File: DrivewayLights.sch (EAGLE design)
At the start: 29 parts, among them U1 TLC59108PW

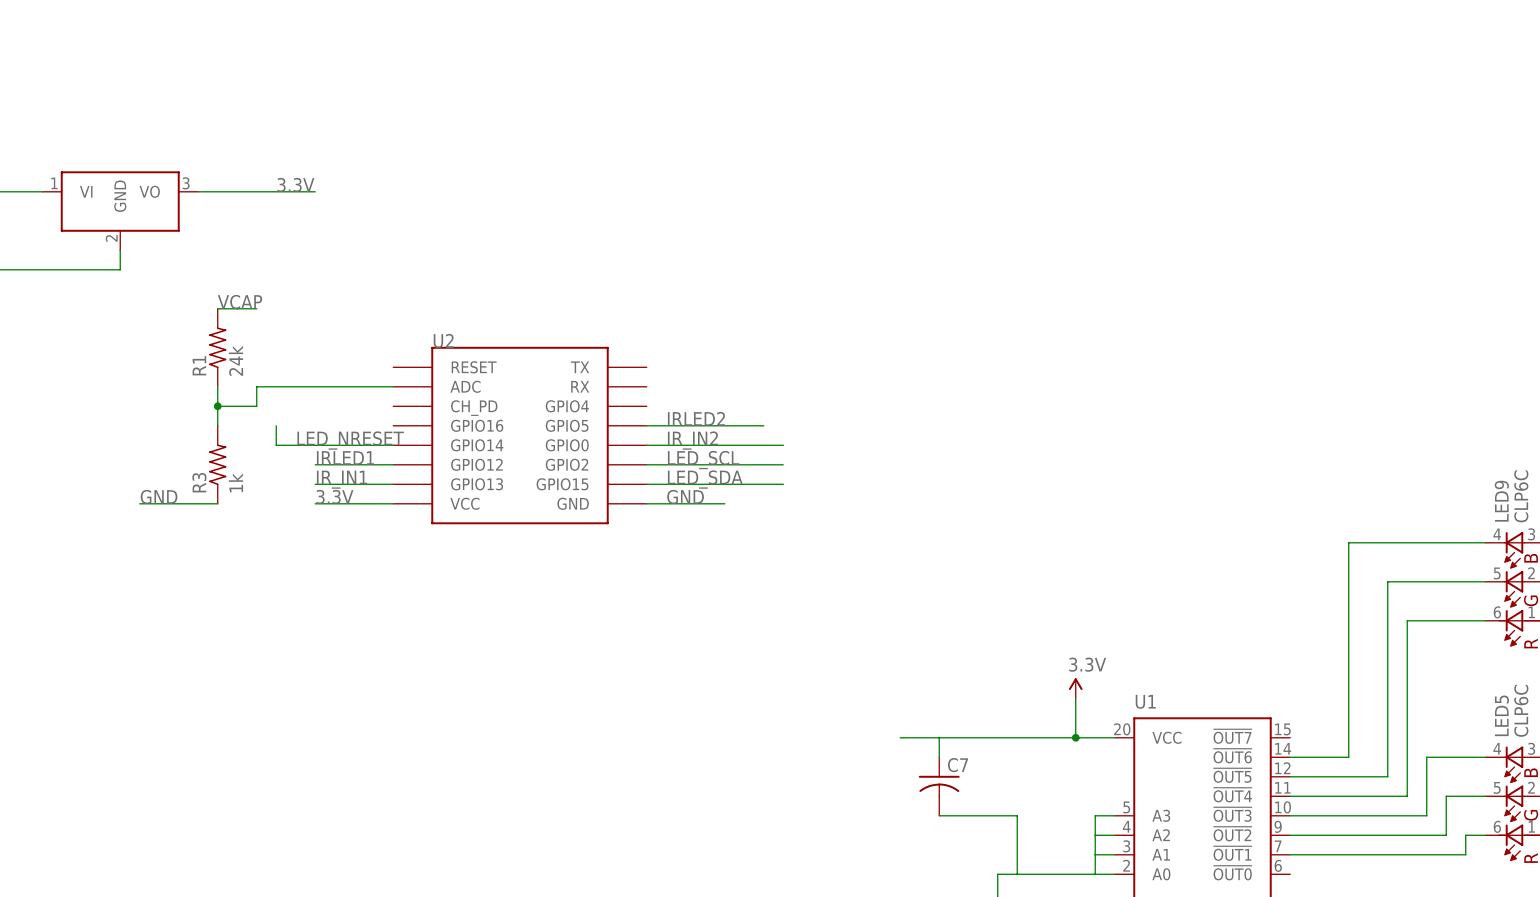
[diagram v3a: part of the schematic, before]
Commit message: Updates to schematic and board layout - a lot of signals ripped up for using correct footprint and adding buttons and interface for programming.
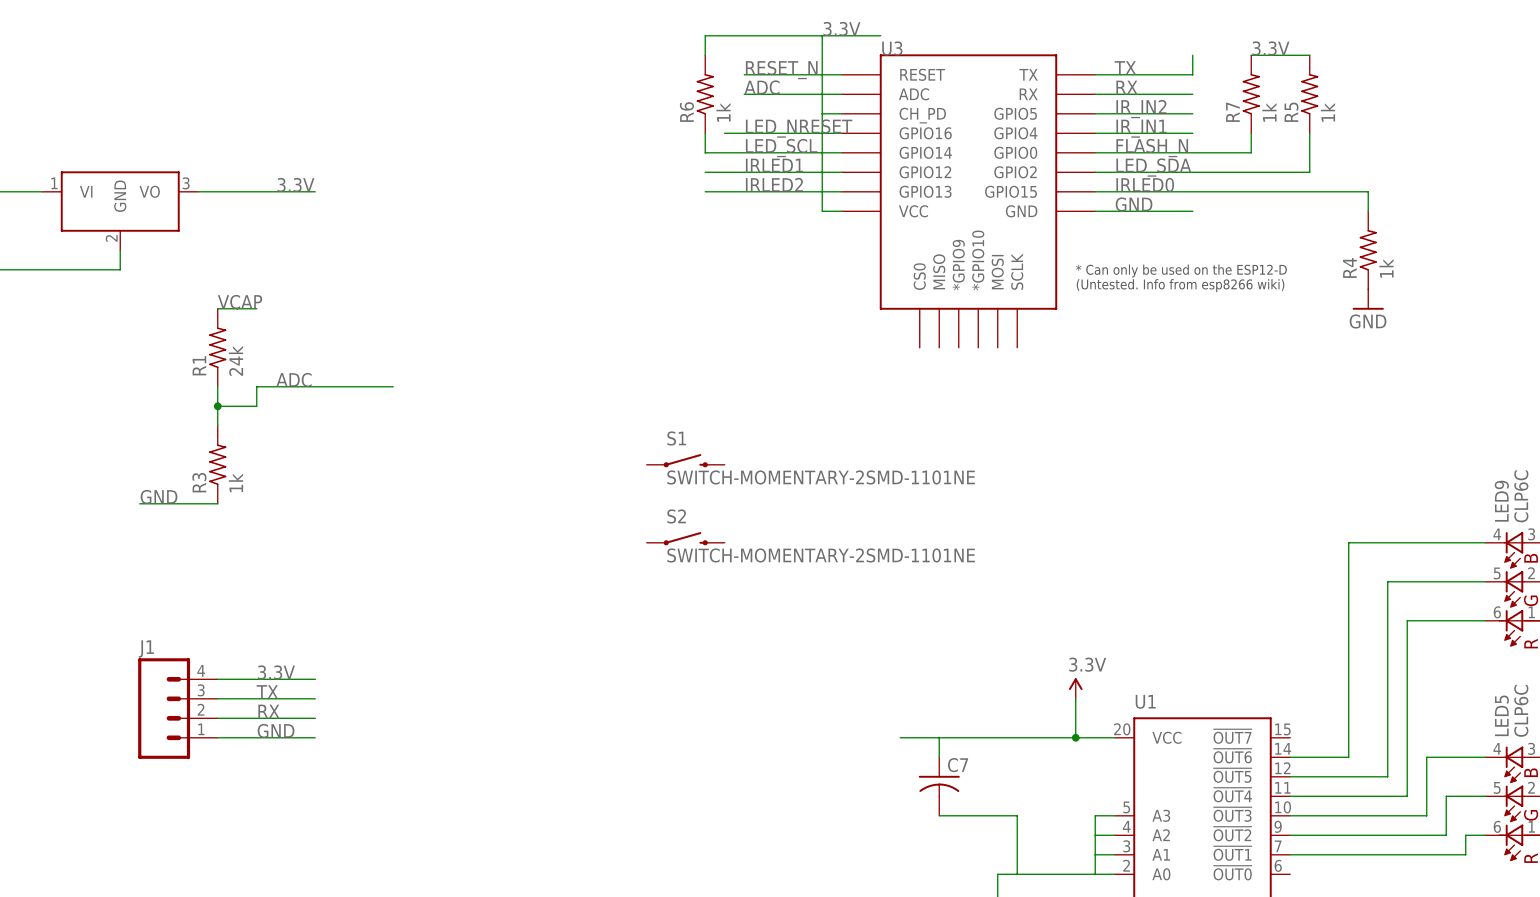
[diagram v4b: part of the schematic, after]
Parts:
- removed U2: (no value), esp8266modules:ESP12SMD
- added J1: (no value), SparkFun-Connectors:M04JST-PTH-VERT
- added R4, R5, R6, R7: 1k, resistor:R-US_R0603
- added S1, S2: SWITCH-MOMENTARY-2SMD-1101NE, SparkFun-Electromechanical:SWITCH-MOMENTARY-2SMD-1101NE
- added U3: (no value), esp8266modules:ESP12ESMD
- T1, T2: EAGLEUP (none) -> SOT23
- U1: EAGLEUP (none) -> TSSOP20
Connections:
- removed net N$7: R1.1, R3.2, U2.ADC
- new net ADC: R1.1, R3.2, U3.ADC
- new net FLASH_N: R7.1, U3.GPIO0
- new net IRLED0: R4.2, U3.GPIO15
- new net RESET_N: U3.RESET
- new net RX: J1.2, U3.RX
- new net TX: J1.3, U3.TX
- net 3.3V: now also J1.4, R5.2, R6.2, R7.2, U3.CH_PD, U3.VCC; no longer U2.VCC
- net GND: now also J1.1, R4.1, U3.GND; no longer U2.GND
- net IRLED1: now also U3.GPIO12; no longer U2.GPIO12
- net IRLED2: now also U3.GPIO13; no longer U2.GPIO5
- net IR_IN1: now also U3.GPIO4; no longer U2.GPIO13
- net IR_IN2: now also U3.GPIO5; no longer U2.GPIO0
- net LED_NRESET: no longer U2.GPIO14
- net LED_SCL: now also R6.1, U3.GPIO14; no longer U2.GPIO2
- net LED_SDA: now also R5.1, U3.GPIO2; no longer U2.GPIO15

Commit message: Added some missing connections on schematic and did some more manual routing
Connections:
- net FLASH_N: now also S1.1
- net GND: now also S1.2, S2.2
- net LED_NRESET: now also U3.GPIO16
- net RESET_N: now also S2.1
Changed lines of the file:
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@@
 <part name="S2" library="SparkFun-Electromechanical" deviceset="SWITCH-MOMENTARY-2" device="SMD-1101NE"/>
 <part name="J1" library="SparkFun-Connectors" deviceset="M04" device="JST-PTH-VERT"/>
+<part name="GND2" library="supply1" deviceset="GND" device=""/>
+<part name="GND3" library="supply1" deviceset="GND" device=""/>
 </parts>
 <sheets>
@@
 <instance part="S2" gate="G$1" x="40.64" y="43.18"/>
 <instance part="J1" gate="G$1" x="-25.4" y="20.32"/>
+<instance part="GND2" gate="1" x="-20.32" y="45.72"/>
+<instance part="GND3" gate="1" x="48.26" y="33.02"/>
 </instances>
 <busses>
@@
 <wire x1="-20.32" y1="48.26" x2="-30.48" y2="48.26" width="0.1524" layer="91"/>
 <label x="-30.48" y="48.26" size="1.778" layer="95"/>
+<pinref part="GND2" gate="1" pin="GND"/>
+<junction x="-20.32" y="48.26"/>
 </segment>
 <segment>
@@
 <wire x1="-20.32" y1="17.78" x2="-7.62" y2="17.78" width="0.1524" layer="91"/>
 <label x="-15.24" y="17.78" size="1.778" layer="95"/>
+</segment>
+<segment>
+<pinref part="GND3" gate="1" pin="GND"/>
+<wire x1="48.26" y1="35.56" x2="48.26" y2="43.18" width="0.1524" layer="91"/>
+<pinref part="S2" gate="G$1" pin="2"/>
+<wire x1="48.26" y1="43.18" x2="45.72" y2="43.18" width="0.1524" layer="91"/>
+<pinref part="S1" gate="G$1" pin="2"/>
+<wire x1="45.72" y1="53.34" x2="48.26" y2="53.34" width="0.1524" layer="91"/>
+<wire x1="48.26" y1="53.34" x2="48.26" y2="43.18" width="0.1524" layer="91"/>
 </segment>
 </net>
@@
 <wire x1="60.96" y1="96.52" x2="45.72" y2="96.52" width="0.1524" layer="91"/>
 <label x="48.26" y="96.52" size="1.778" layer="95"/>
+<pinref part="U3" gate="G$1" pin="GPIO16"/>
 </segment>
 </net>
@@
 <wire x1="114.3" y1="93.98" x2="114.3" y2="96.52" width="0.1524" layer="91"/>
 </segment>
+<segment>
+<pinref part="S1" gate="G$1" pin="1"/>
+<wire x1="35.56" y1="53.34" x2="22.86" y2="53.34" width="0.1524" layer="91"/>
+<label x="25.4" y="53.34" size="1.778" layer="95"/>
+</segment>
 </net>
 <net name="RESET_N" class="0">
@@
 <label x="48.26" y="104.14" size="1.778" layer="95"/>
 </segment>
-</net>
+<segment>
+<pinref part="S2" gate="G$1" pin="1"/>
+<wire x1="35.56" y1="43.18" x2="22.86" y2="43.18" width="0.1524" layer="91"/>
+<label x="25.4" y="43.18" size="1.778" layer="95"/>
+</segment>
+</net>

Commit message: Updates to board layout to bring dimensions back into where they should probably be.  Need to route board again, but hopefully this will now be good assuming the schematic is right.  Also capturing last rounds models and 3d print files
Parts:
- removed S1, S2: SWITCH-MOMENTARY-2SMD-1101NE, SparkFun-Electromechanical:SWITCH-MOMENTARY-2SMD-1101NE
- added S3, S4: SWITCH-MOMENTARY-2SMD, SparkFun-Electromechanical:SWITCH-MOMENTARY-2SMD
- LED10, LED11, LED12, LED5, LED6, LED7, LED8, LED9: EAGLEUP (none) -> PLCC-6-LED
- U3: EAGLEUP (none) -> ESP8266-12E
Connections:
- net FLASH_N: now also S3.1; no longer S1.1
- net GND: now also S3.2, S4.2; no longer S1.2, S2.2
- net RESET_N: now also S4.1; no longer S2.1
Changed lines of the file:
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@@
 <part name="GND10" library="supply1" deviceset="GND" device=""/>
 <part name="R2" library="rcl" deviceset="R-US_" device="R0603" value="625"/>
-<part name="LED5" library="led" deviceset="CLP6C" device=""/>
-<part name="LED6" library="led" deviceset="CLP6C" device=""/>
-<part name="LED7" library="led" deviceset="CLP6C" device=""/>
-<part name="LED8" library="led" deviceset="CLP6C" device=""/>
+<part name="LED5" library="led" deviceset="CLP6C" device="">
+<attribute name="EAGLEUP" value="PLCC-6-LED"/>
+</part>
+<part name="LED6" library="led" deviceset="CLP6C" device="">
+<attribute name="EAGLEUP" value="PLCC-6-LED"/>
+</part>
+<part name="LED7" library="led" deviceset="CLP6C" device="">
+<attribute name="EAGLEUP" value="PLCC-6-LED"/>
+</part>
+<part name="LED8" library="led" deviceset="CLP6C" device="">
+<attribute name="EAGLEUP" value="PLCC-6-LED"/>
+</part>
 <part name="J11" library="con-amp" deviceset="MTA02-100" device=""/>
 <part name="GND15" library="supply1" deviceset="GND" device=""/>
@@
 <part name="GND17" library="supply1" deviceset="GND" device=""/>
 <part name="C7" library="rcl" deviceset="C-US" device="C0603"/>
-<part name="LED9" library="led" deviceset="CLP6C" device=""/>
-<part name="LED10" library="led" deviceset="CLP6C" device=""/>
-<part name="LED11" library="led" deviceset="CLP6C" device=""/>
-<part name="LED12" library="led" deviceset="CLP6C" device=""/>
+<part name="LED9" library="led" deviceset="CLP6C" device="">
+<attribute name="EAGLEUP" value="PLCC-6-LED"/>
+</part>
+<part name="LED10" library="led" deviceset="CLP6C" device="">
+<attribute name="EAGLEUP" value="PLCC-6-LED"/>
+</part>
+<part name="LED11" library="led" deviceset="CLP6C" device="">
+<attribute name="EAGLEUP" value="PLCC-6-LED"/>
+</part>
+<part name="LED12" library="led" deviceset="CLP6C" device="">
+<attribute name="EAGLEUP" value="PLCC-6-LED"/>
+</part>
 <part name="B1" library="rectifier" deviceset="B*S" device="" technology="6"/>
 <part name="GND20" library="supply1" deviceset="GND" device=""/>
@@
 <part name="R1" library="resistor" deviceset="R-US_" device="R0603" value="24k"/>
 <part name="R3" library="resistor" deviceset="R-US_" device="R0603" value="1k"/>
-<part name="U3" library="esp8266modules" deviceset="ESP12E" device="SMD"/>
+<part name="U3" library="esp8266modules" deviceset="ESP12E" device="SMD">
+<attribute name="EAGLEUP" value="ESP8266-12E"/>
+</part>
 <part name="R4" library="resistor" deviceset="R-US_" device="R0603" value="1k"/>
 <part name="R5" library="resistor" deviceset="R-US_" device="R0603" value="1k"/>
@@
 <part name="R7" library="resistor" deviceset="R-US_" device="R0603" value="1k"/>
 <part name="GND1" library="supply1" deviceset="GND" device=""/>
-<part name="S1" library="SparkFun-Electromechanical" deviceset="SWITCH-MOMENTARY-2" device="SMD-1101NE"/>
-<part name="S2" library="SparkFun-Electromechanical" deviceset="SWITCH-MOMENTARY-2" device="SMD-1101NE"/>
 <part name="J1" library="SparkFun-Connectors" deviceset="M04" device="JST-PTH-VERT"/>
 <part name="GND2" library="supply1" deviceset="GND" device=""/>
 <part name="GND3" library="supply1" deviceset="GND" device=""/>
+<part name="S3" library="SparkFun-Electromechanical" deviceset="SWITCH-MOMENTARY-2" device="SMD"/>
+<part name="S4" library="SparkFun-Electromechanical" deviceset="SWITCH-MOMENTARY-2" device="SMD"/>
 </parts>
 <sheets>
@@
 <instance part="GND10" gate="1" x="81.28" y="-7.62"/>
 <instance part="R2" gate="G$1" x="124.46" y="-15.24" rot="R90"/>
-<instance part="LED5" gate="G$1" x="149.86" y="10.16" rot="MR90"/>
-<instance part="LED6" gate="G$1" x="180.34" y="10.16" rot="MR90"/>
-<instance part="LED7" gate="G$1" x="170.18" y="10.16" rot="MR90"/>
-<instance part="LED8" gate="G$1" x="160.02" y="10.16" rot="MR90"/>
+<instance part="LED5" gate="G$1" x="149.86" y="10.16" rot="MR90">
+<attribute name="EAGLEUP" x="149.86" y="10.16" size="1.778" layer="96" rot="MR90" display="off"/>
+</instance>
+<instance part="LED6" gate="G$1" x="180.34" y="10.16" rot="MR90">
+<attribute name="EAGLEUP" x="180.34" y="10.16" size="1.778" layer="96" rot="MR90" display="off"/>
+</instance>
+<instance part="LED7" gate="G$1" x="170.18" y="10.16" rot="MR90">
+<attribute name="EAGLEUP" x="170.18" y="10.16" size="1.778" layer="96" rot="MR90" display="off"/>
+</instance>
+<instance part="LED8" gate="G$1" x="160.02" y="10.16" rot="MR90">
+<attribute name="EAGLEUP" x="160.02" y="10.16" size="1.778" layer="96" rot="MR90" display="off"/>
+</instance>
 <instance part="J11" gate="G$1" x="-111.76" y="91.44" rot="R90"/>
 <instance part="GND15" gate="1" x="124.46" y="-53.34"/>
@@
 <instance part="GND17" gate="1" x="40.64" y="-88.9"/>
 <instance part="C7" gate="G$1" x="73.66" y="12.7"/>
-<instance part="LED9" gate="G$1" x="149.86" y="38.1" rot="MR90"/>
-<instance part="LED10" gate="G$1" x="180.34" y="38.1" rot="MR90"/>
-<instance part="LED11" gate="G$1" x="170.18" y="38.1" rot="MR90"/>
-<instance part="LED12" gate="G$1" x="160.02" y="38.1" rot="MR90"/>
+<instance part="LED9" gate="G$1" x="149.86" y="38.1" rot="MR90">
+<attribute name="EAGLEUP" x="149.86" y="38.1" size="1.778" layer="96" rot="MR90" display="off"/>
+</instance>
+<instance part="LED10" gate="G$1" x="180.34" y="38.1" rot="MR90">
+<attribute name="EAGLEUP" x="180.34" y="38.1" size="1.778" layer="96" rot="MR90" display="off"/>
+</instance>
+<instance part="LED11" gate="G$1" x="170.18" y="38.1" rot="MR90">
+<attribute name="EAGLEUP" x="170.18" y="38.1" size="1.778" layer="96" rot="MR90" display="off"/>
+</instance>
+<instance part="LED12" gate="G$1" x="160.02" y="38.1" rot="MR90">
+<attribute name="EAGLEUP" x="160.02" y="38.1" size="1.778" layer="96" rot="MR90" display="off"/>
+</instance>
 <instance part="B1" gate="G$1" x="-88.9" y="88.9"/>
 <instance part="GND20" gate="1" x="-99.06" y="83.82"/>
@@
 <instance part="R1" gate="G$1" x="-20.32" y="68.58" rot="R90"/>
 <instance part="R3" gate="G$1" x="-20.32" y="53.34" rot="R90"/>
-<instance part="U3" gate="G$1" x="78.74" y="96.52"/>
+<instance part="U3" gate="G$1" x="78.74" y="96.52">
+<attribute name="EAGLEUP" x="78.74" y="96.52" size="1.778" layer="96" display="off"/>
+</instance>
 <instance part="R4" gate="G$1" x="129.54" y="81.28" rot="R90"/>
 <instance part="R5" gate="G$1" x="121.92" y="101.6" rot="R90"/>
@@
 <instance part="R7" gate="G$1" x="114.3" y="101.6" rot="R90"/>
 <instance part="GND1" gate="1" x="129.54" y="73.66"/>
-<instance part="S1" gate="G$1" x="40.64" y="53.34"/>
-<instance part="S2" gate="G$1" x="40.64" y="43.18"/>
 <instance part="J1" gate="G$1" x="-25.4" y="20.32"/>
 <instance part="GND2" gate="1" x="-20.32" y="45.72"/>
 <instance part="GND3" gate="1" x="48.26" y="33.02"/>
+<instance part="S3" gate="G$1" x="40.64" y="53.34"/>
+<instance part="S4" gate="G$1" x="40.64" y="43.18"/>
 </instances>
 <busses>
@@
 <pinref part="GND3" gate="1" pin="GND"/>
 <wire x1="48.26" y1="35.56" x2="48.26" y2="43.18" width="0.1524" layer="91"/>
-<pinref part="S2" gate="G$1" pin="2"/>
 <wire x1="48.26" y1="43.18" x2="45.72" y2="43.18" width="0.1524" layer="91"/>
-<pinref part="S1" gate="G$1" pin="2"/>
 <wire x1="45.72" y1="53.34" x2="48.26" y2="53.34" width="0.1524" layer="91"/>
 <wire x1="48.26" y1="53.34" x2="48.26" y2="43.18" width="0.1524" layer="91"/>
+<pinref part="S3" gate="G$1" pin="2"/>
+<pinref part="S4" gate="G$1" pin="2"/>
 </segment>
 </net>
@@
 </segment>
 <segment>
-<pinref part="S1" gate="G$1" pin="1"/>
 <wire x1="35.56" y1="53.34" x2="22.86" y2="53.34" width="0.1524" layer="91"/>
 <label x="25.4" y="53.34" size="1.778" layer="95"/>
+<pinref part="S3" gate="G$1" pin="1"/>
 </segment>
 </net>
@@
 </segment>
 <segment>
-<pinref part="S2" gate="G$1" pin="1"/>
 <wire x1="35.56" y1="43.18" x2="22.86" y2="43.18" width="0.1524" layer="91"/>
 <label x="25.4" y="43.18" size="1.778" layer="95"/>
-</segment>
-</net>
+<pinref part="S4" gate="G$1" pin="1"/>
+</segment>
+</net>

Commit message: Updates to schematic and relayout board
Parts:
- removed R6: 1k, resistor:R-US_R0603
- added R10, R9: 10k, resistor:R-US_R0603
- added R8: 1k, resistor:R-US_R0603
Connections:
- new net BLUE_LED: R5.1, U3.GPIO2
- net 3.3V: now also R10.2, R8.2, R9.2; no longer R6.2
- net IR_IN1: now also U3.GPIO14; no longer U3.GPIO4
- net IR_IN2: now also U3.GPIO16; no longer U3.GPIO5
- net LED_NRESET: now also R8.1; no longer U3.GPIO16
- net LED_SCL: now also R10.1, U3.GPIO5; no longer R6.1, U3.GPIO14
- net LED_SDA: now also R9.1, U3.GPIO4; no longer R5.1, U3.GPIO2
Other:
- moved on the sheet: R5, R7

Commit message: Renamed parts and cleaned up silkscreen on board to prepare for next build
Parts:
- removed LED10, LED11, LED12, LED9: CLP6C, led:CLP6C
- removed R13, R14: 10, rcl:R-US_R0603
- removed U$4: DCDC_OKI-78SR, rwt-library:DCDC_OKI-78SR
- added LED1, LED2, LED3, LED4: CLP6C, led:CLP6C
- added R11: 625, rcl:R-US_R0603
- added R6: 10k, resistor:R-US_R0603
- added U2: TLC59108PW, texas:TLC59108PW
- R10, R9: value 10k -> 10; device resistor:R-US_R0603 -> rcl:R-US_R0603
- R2: value 625 -> 1k; device rcl:R-US_R0603 -> resistor:R-US_R0603
- R7: value 1k -> 10k
- U1: value TLC59108PW -> (none); device texas:TLC59108PW -> esp8266modules:ESP12ESMD; EAGLEUP TSSOP20 -> ESP8266-12E
- U3: value (none) -> DCDC_OKI-78SR; device esp8266modules:ESP12ESMD -> rwt-library:DCDC_OKI-78SR; EAGLEUP ESP8266-12E -> (none)
- renumbered C10 to C5, C11 to C2, C7 to C3, C9 to C4, J11 to J2, U$1 to U4, U$2 to U5
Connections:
- net 3.3V: now also R3.2, R6.2, U1.CH_PD, U2.VCC, U3.VO; no longer R10.2, R9.2, U$4.VO, U3.CH_PD, U3.VCC
- net ADC: now also R2.2, U1.ADC; no longer R3.2, U3.ADC
- net BLUE: now also LED1.BC, U2.!OUT3; no longer LED5.BC, U1.!OUT3
- net BLUE2: now also LED5.BC, U2.!OUT6; no longer LED9.BC, U1.!OUT6
- net BLUE_LED: now also R3.1, U1.GPIO2; no longer R5.1, U3.GPIO2
- net FLASH_N: now also R5.1, U1.GPIO0; no longer R7.1, U3.GPIO0
- net GND: now also R11.1, U2.A0, U2.A1, U2.A2, U2.A3, U2.GND; no longer R3.1, U$4.GND, U1.A0, U1.A1, U1.A2, U1.A3
- net GREEN: now also LED1.GC, U2.!OUT2; no longer LED5.GC, U1.!OUT2
- net GREEN2: now also LED5.GC, U2.!OUT5; no longer LED9.GC, U1.!OUT5
- net IRLED0: now also U1.GPIO15; no longer U3.GPIO15
- net IRLED1: now also U1.GPIO12; no longer U3.GPIO12
- net IRLED2: now also U1.GPIO13; no longer U3.GPIO13
- net IR_IN1: now also U1.GPIO14; no longer U3.GPIO14
- net IR_IN2: now also U1.GPIO16; no longer U3.GPIO16
- net LED_CURRENT_R: now also R11.2, U2.REXT; no longer R2.2, U1.REXT
- net LED_NRESET: now also U2.!RESET; no longer U1.!RESET
- net LED_SCL: now also R7.1, U1.GPIO5, U2.SCL; no longer R10.1, U1.SCL, U3.GPIO5
- net LED_SDA: now also R6.1, U1.GPIO4, U2.SDA; no longer R9.1, U1.SDA, U3.GPIO4
- net N$12: now also LED5.BA, LED6.BC; no longer LED12.BC, LED9.BA
- net N$13: now also LED6.BA, LED7.BC; no longer LED11.BC, LED12.BA
- net N$14: now also LED7.BA, LED8.BC; no longer LED10.BC, LED11.BA
- net N$15: now also LED7.GA, LED8.GC; no longer LED10.GC, LED11.GA
- net N$16: now also LED6.GA, LED7.GC; no longer LED11.GC, LED12.GA
- net N$17: now also LED5.GA, LED6.GC; no longer LED12.GC, LED9.GA
- net N$18: now also LED5.RA, LED6.RC; no longer LED12.RC, LED9.RA
- net N$2: now also R9.2; no longer R14.2
- net N$20: now also LED6.RA, LED7.RC; no longer LED11.RC, LED12.RA
- net N$21: now also LED7.RA, LED8.RC; no longer LED10.RC, LED11.RA
- net N$25: now also LED1.BA, LED2.BC; no longer LED5.BA, LED8.BC
- net N$26: now also LED2.BA, LED3.BC; no longer LED7.BC, LED8.BA
- net N$27: now also LED3.BA, LED4.BC; no longer LED6.BC, LED7.BA
- net N$28: now also LED3.GA, LED4.GC; no longer LED6.GC, LED7.GA
- net N$29: now also LED2.GA, LED3.GC; no longer LED7.GC, LED8.GA
- net N$30: now also LED1.GA, LED2.GC; no longer LED5.GA, LED8.GC
- net N$31: now also LED1.RA, LED2.RC; no longer LED5.RA, LED8.RC
- net N$32: now also LED2.RA, LED3.RC; no longer LED7.RC, LED8.RA
- net N$33: now also LED3.RA, LED4.RC; no longer LED6.RC, LED7.RA
- net N$5: now also R10.2; no longer R13.2
- net N$6: now also R10.1; no longer R13.1
- net N$9: now also R9.1; no longer R14.1
- net RED: now also LED1.RC, U2.!OUT1; no longer LED5.RC, U1.!OUT1
- net RED2: now also LED5.RC, U2.!OUT4; no longer LED9.RC, U1.!OUT4
- net RESET_N: now also U1.RESET; no longer U3.RESET
- net RX: now also U1.RX; no longer U3.RX
- net TX: now also U1.TX; no longer U3.TX
- net VCAP: now also LED4.BA, LED4.GA, LED4.RA, LED8.BA, LED8.GA, LED8.RA, U3.VI; no longer LED10.BA, LED10.GA, LED10.RA, LED6.BA, LED6.GA, LED6.RA, U$4.VI
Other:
- moved on the sheet: LED5, LED6, LED7, LED8, R10, R2, R3, R5, R7, R9
